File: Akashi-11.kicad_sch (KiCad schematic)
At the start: 45 parts, among them CN10 PPPC192LFBN-RC, CN7 PPPC192LFBN-RC, J1 Conn_02x20_Odd_Even, SW1 SW, U1 MAX6934AQH+D, U2 MAX4719EUB+, U3 TPS613221ADBV, U4 TLV61046ADB

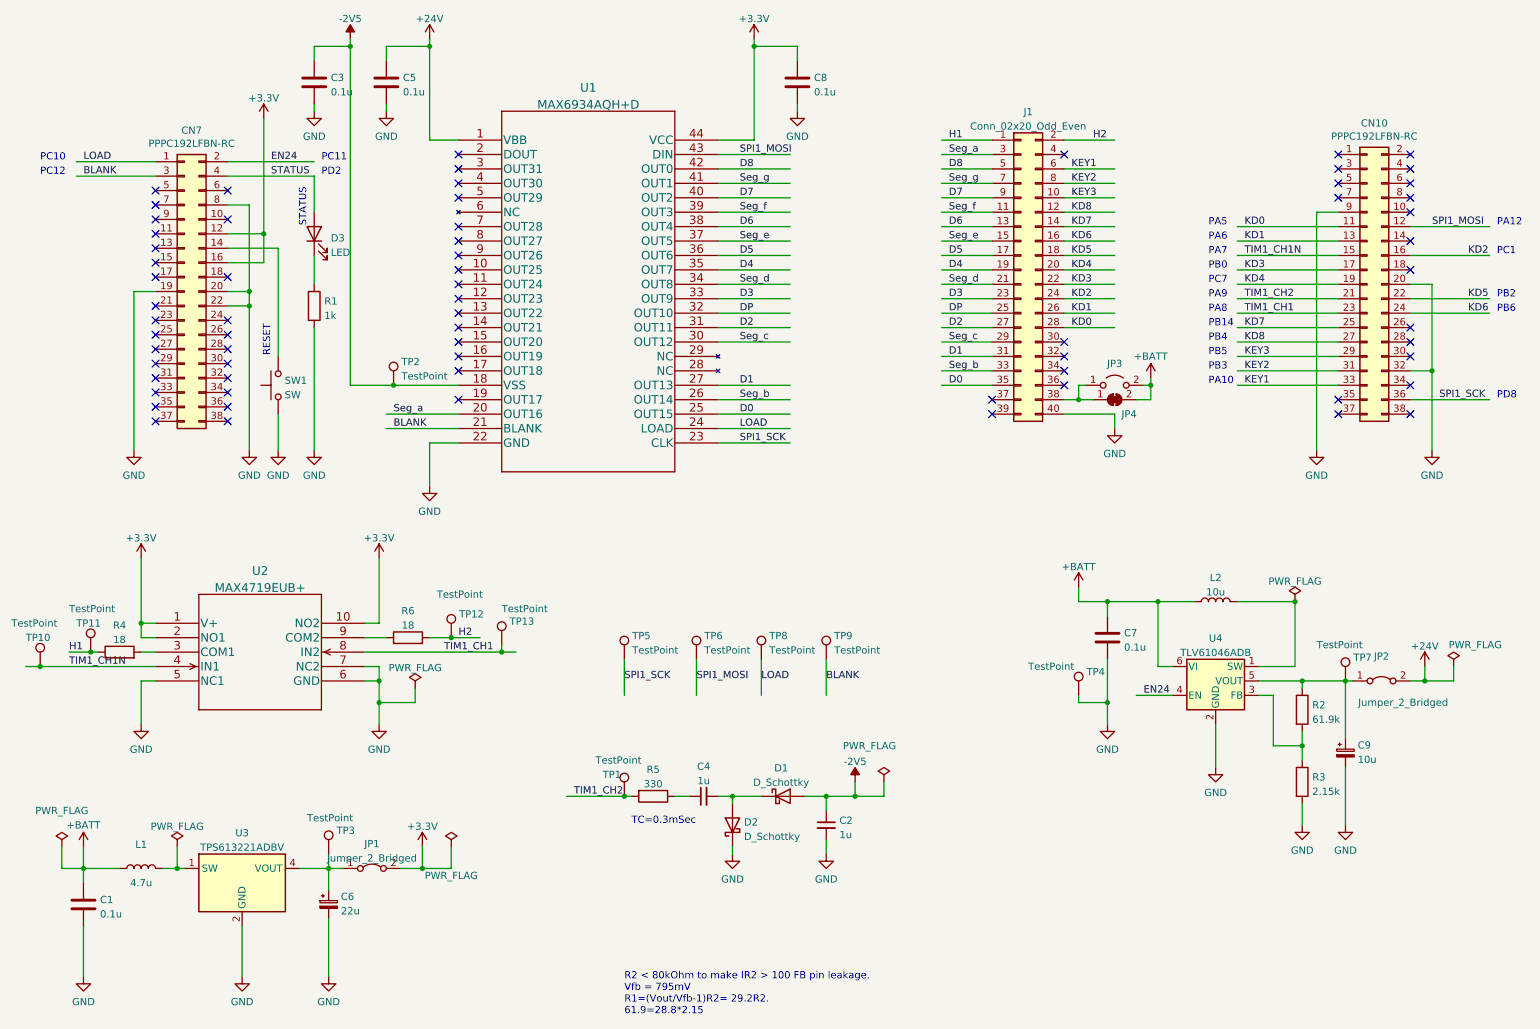
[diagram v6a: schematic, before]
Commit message: Modified schematics and silk.
- KEY matrix signal name is changed.
-- Including bug fix of the row order.
- R5 is changed to small resiter to fix the to small voltage.

Gerber re-generated. Schematics re-generated in PDF.
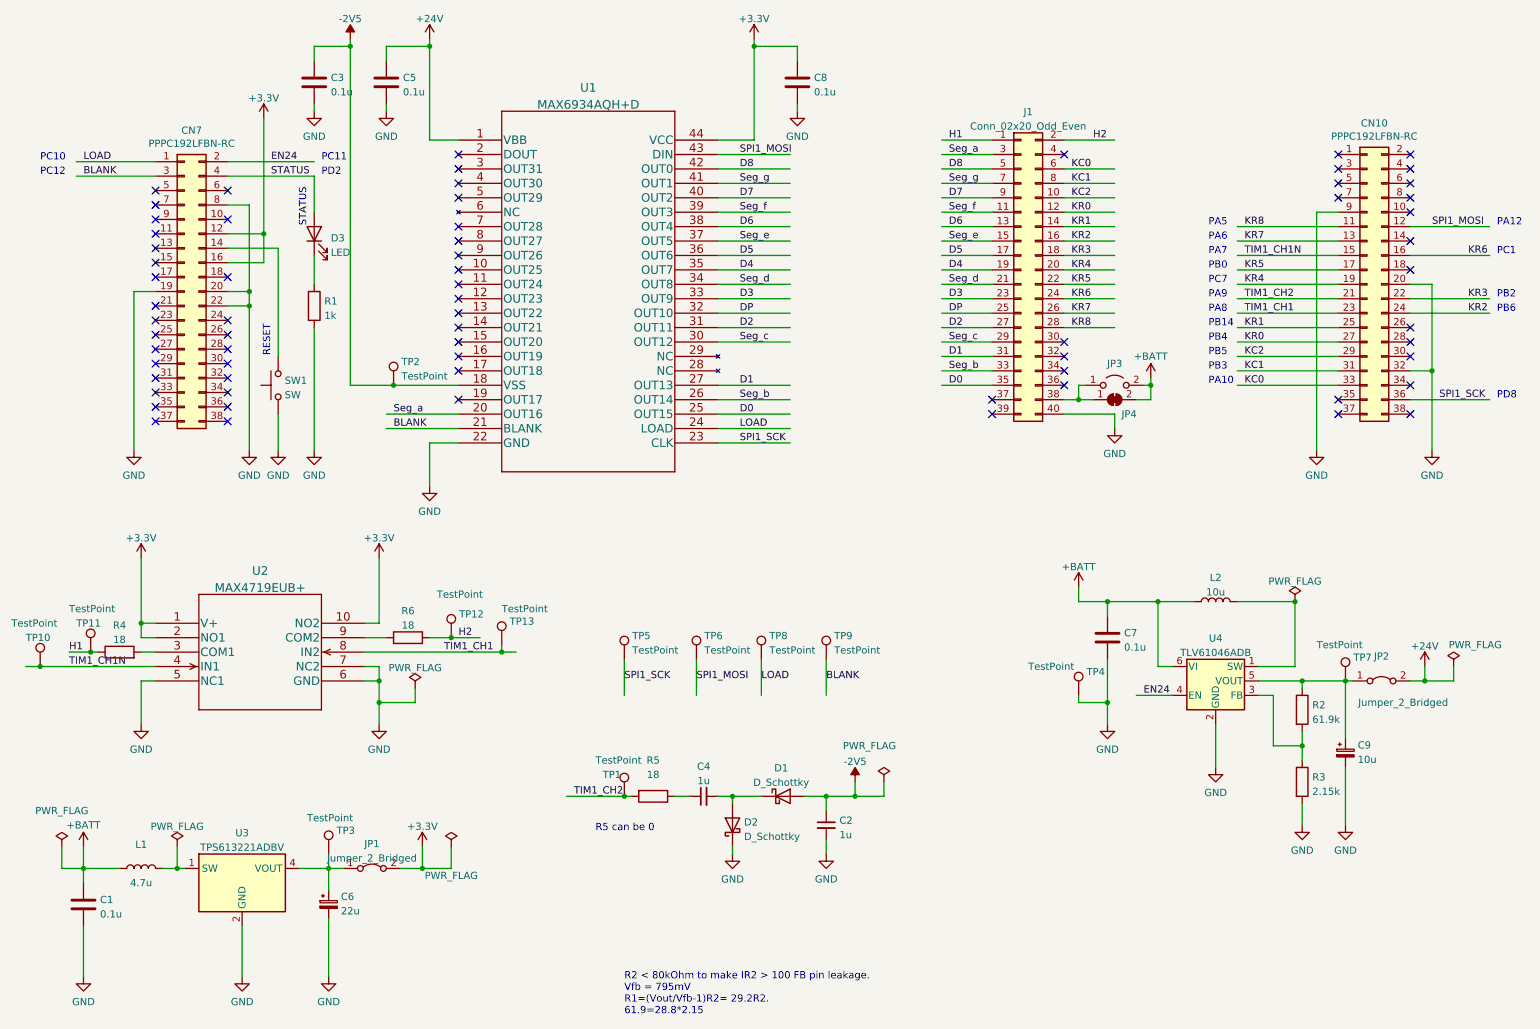
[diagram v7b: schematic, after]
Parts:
- R5: value 330 -> 18
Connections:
- net KD0 renamed KR8
- net KD1 renamed KR7
- net KD2 renamed KR6
- net KD3 renamed KR5
- net KD4 renamed KR4
- net KD5 renamed KR3
- net KD6 renamed KR2
- net KD7 renamed KR1
- net KD8 renamed KR0
- net KEY1 renamed KC0
- net KEY2 renamed KC1
- net KEY3 renamed KC2
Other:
- note added: "R5 can be 0"
- note removed: "TC=0.3mSec"
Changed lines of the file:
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@@
     (effects (font (size 1.27 1.27)) (justify left bottom))
   )
-  (text "TC=0.3mSec" (at 123.19 157.48 0)
+  (text "R5 can be 0" (at 116.84 158.75 0)
     (effects (font (size 1.27 1.27)) (justify left bottom))
   )
@@
     (effects (font (size 1.27 1.27)) (justify left bottom))
   )
-  (label "KD6" (at 200.66 54.61 0)
+  (label "KR2" (at 200.66 54.61 0)
     (effects (font (size 1.27 1.27)) (justify left bottom))
   )
@@
     (effects (font (size 1.27 1.27)) (justify left bottom))
   )
-  (label "KD8" (at 200.66 49.53 0)
-    (effects (font (size 1.27 1.27)) (justify left bottom))
-  )
-  (label "KD2" (at 270.51 57.15 0)
-    (effects (font (size 1.27 1.27)) (justify left bottom))
-  )
-  (label "KEY1" (at 200.66 41.91 0)
+  (label "KR0" (at 200.66 49.53 0)
+    (effects (font (size 1.27 1.27)) (justify left bottom))
+  )
+  (label "KR6" (at 270.51 57.15 0)
+    (effects (font (size 1.27 1.27)) (justify left bottom))
+  )
+  (label "KC0" (at 200.66 41.91 0)
     (effects (font (size 1.27 1.27)) (justify left bottom))
   )
@@
     (effects (font (size 1.27 1.27)) (justify left bottom))
   )
-  (label "KD5" (at 200.66 57.15 0)
-    (effects (font (size 1.27 1.27)) (justify left bottom))
-  )
-  (label "KD1" (at 200.66 67.31 0)
-    (effects (font (size 1.27 1.27)) (justify left bottom))
-  )
-  (label "KD3" (at 200.66 62.23 0)
+  (label "KR3" (at 200.66 57.15 0)
+    (effects (font (size 1.27 1.27)) (justify left bottom))
+  )
+  (label "KR7" (at 200.66 67.31 0)
+    (effects (font (size 1.27 1.27)) (justify left bottom))
+  )
+  (label "KR5" (at 200.66 62.23 0)
     (effects (font (size 1.27 1.27)) (justify left bottom))
   )
@@
     (effects (font (size 1.27 1.27)) (justify left bottom))
   )
-  (label "KEY2" (at 231.14 77.47 0)
+  (label "KC1" (at 231.14 77.47 0)
     (effects (font (size 1.27 1.27)) (justify left bottom))
   )
@@
     (effects (font (size 1.27 1.27)) (justify left bottom))
   )
-  (label "KD3" (at 231.14 59.69 0)
+  (label "KR5" (at 231.14 59.69 0)
     (effects (font (size 1.27 1.27)) (justify left bottom))
   )
@@
     (effects (font (size 1.27 1.27)) (justify left bottom))
   )
-  (label "KD7" (at 231.14 69.85 0)
+  (label "KR1" (at 231.14 69.85 0)
     (effects (font (size 1.27 1.27)) (justify left bottom))
   )
@@
     (effects (font (size 1.27 1.27)) (justify left bottom))
   )
-  (label "KEY3" (at 231.14 74.93 0)
+  (label "KC2" (at 231.14 74.93 0)
     (effects (font (size 1.27 1.27)) (justify left bottom))
   )
@@
     (effects (font (size 1.27 1.27)) (justify left bottom))
   )
-  (label "KD4" (at 200.66 59.69 0)
-    (effects (font (size 1.27 1.27)) (justify left bottom))
-  )
-  (label "KEY1" (at 231.14 80.01 0)
+  (label "KR4" (at 200.66 59.69 0)
+    (effects (font (size 1.27 1.27)) (justify left bottom))
+  )
+  (label "KC0" (at 231.14 80.01 0)
     (effects (font (size 1.27 1.27)) (justify left bottom))
   )
@@
     (effects (font (size 1.27 1.27)) (justify left bottom))
   )
-  (label "KD0" (at 200.66 69.85 0)
+  (label "KR8" (at 200.66 69.85 0)
     (effects (font (size 1.27 1.27)) (justify left bottom))
   )
@@
     (effects (font (size 1.27 1.27)) (justify left bottom))
   )
-  (label "KEY3" (at 200.66 46.99 0)
+  (label "KC2" (at 200.66 46.99 0)
     (effects (font (size 1.27 1.27)) (justify left bottom))
   )
@@
     (effects (font (size 1.27 1.27)) (justify left bottom))
   )
-  (label "KD1" (at 231.14 54.61 0)
+  (label "KR7" (at 231.14 54.61 0)
     (effects (font (size 1.27 1.27)) (justify left bottom))
   )
@@
     (effects (font (size 1.27 1.27)) (justify left bottom))
   )
-  (label "KD5" (at 270.51 64.77 0)
+  (label "KR3" (at 270.51 64.77 0)
     (effects (font (size 1.27 1.27)) (justify left bottom))
   )
@@
     (effects (font (size 1.27 1.27)) (justify left bottom))
   )
-  (label "KD0" (at 231.14 52.07 0)
+  (label "KR8" (at 231.14 52.07 0)
     (effects (font (size 1.27 1.27)) (justify left bottom))
   )
@@
     (effects (font (size 1.27 1.27)) (justify left bottom))
   )
-  (label "KD2" (at 200.66 64.77 0)
-    (effects (font (size 1.27 1.27)) (justify left bottom))
-  )
-  (label "KD6" (at 270.51 67.31 0)
+  (label "KR6" (at 200.66 64.77 0)
+    (effects (font (size 1.27 1.27)) (justify left bottom))
+  )
+  (label "KR2" (at 270.51 67.31 0)
     (effects (font (size 1.27 1.27)) (justify left bottom))
   )
@@
     (effects (font (size 1.27 1.27)) (justify left bottom))
   )
-  (label "KD7" (at 200.66 52.07 0)
+  (label "KR1" (at 200.66 52.07 0)
     (effects (font (size 1.27 1.27)) (justify left bottom))
   )
@@
     (effects (font (size 1.27 1.27)) (justify left bottom))
   )
-  (label "KEY2" (at 200.66 44.45 0)
+  (label "KC1" (at 200.66 44.45 0)
     (effects (font (size 1.27 1.27)) (justify left bottom))
   )
@@
     (effects (font (size 1.27 1.27)) (justify left bottom))
   )
-  (label "KD4" (at 231.14 62.23 0)
-    (effects (font (size 1.27 1.27)) (justify left bottom))
-  )
-  (label "KD8" (at 231.14 72.39 0)
+  (label "KR4" (at 231.14 62.23 0)
+    (effects (font (size 1.27 1.27)) (justify left bottom))
+  )
+  (label "KR0" (at 231.14 72.39 0)
     (effects (font (size 1.27 1.27)) (justify left bottom))
   )
@@
   (symbol (lib_id "Device:R") (at 127 152.4 270) (unit 1)
     (in_bom yes) (on_board yes) (fields_autoplaced)
-    (property "Reference" "R5" (id 0) (at 127 147.6842 90))
-    (property "Value" "330" (id 1) (at 127 150.2211 90))
+    (property "Reference" "R5" (id 0) (at 127 146.05 90))
+    (property "Value" "18" (id 1) (at 127 148.59 90))
     (property "Footprint" "Capacitor_SMD:C_0603_1608Metric_Pad1.08x0.95mm_HandSolder" (id 2) (at 127 150.622 90)
       (effects (font (size 1.27 1.27)) hide)
@@
     )
     (path "/df2d9c9f-cb48-424c-9647-501642b6bc8d"
-      (reference "R5") (unit 1) (value "330") (footprint "Capacitor_SMD:C_0603_1608Metric_Pad1.08x0.95mm_HandSolder")
+      (reference "R5") (unit 1) (value "18") (footprint "Capacitor_SMD:C_0603_1608Metric_Pad1.08x0.95mm_HandSolder")
     )
     (path "/8ce81ab9-7f4c-4250-a09f-443d5117f2dc"
